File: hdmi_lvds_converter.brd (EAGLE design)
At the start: 100 x 50 mm, 3 parts, among them J602 SS-53000-001, U1 DS90C387VJD/NOPB, U2 TFP401APZP

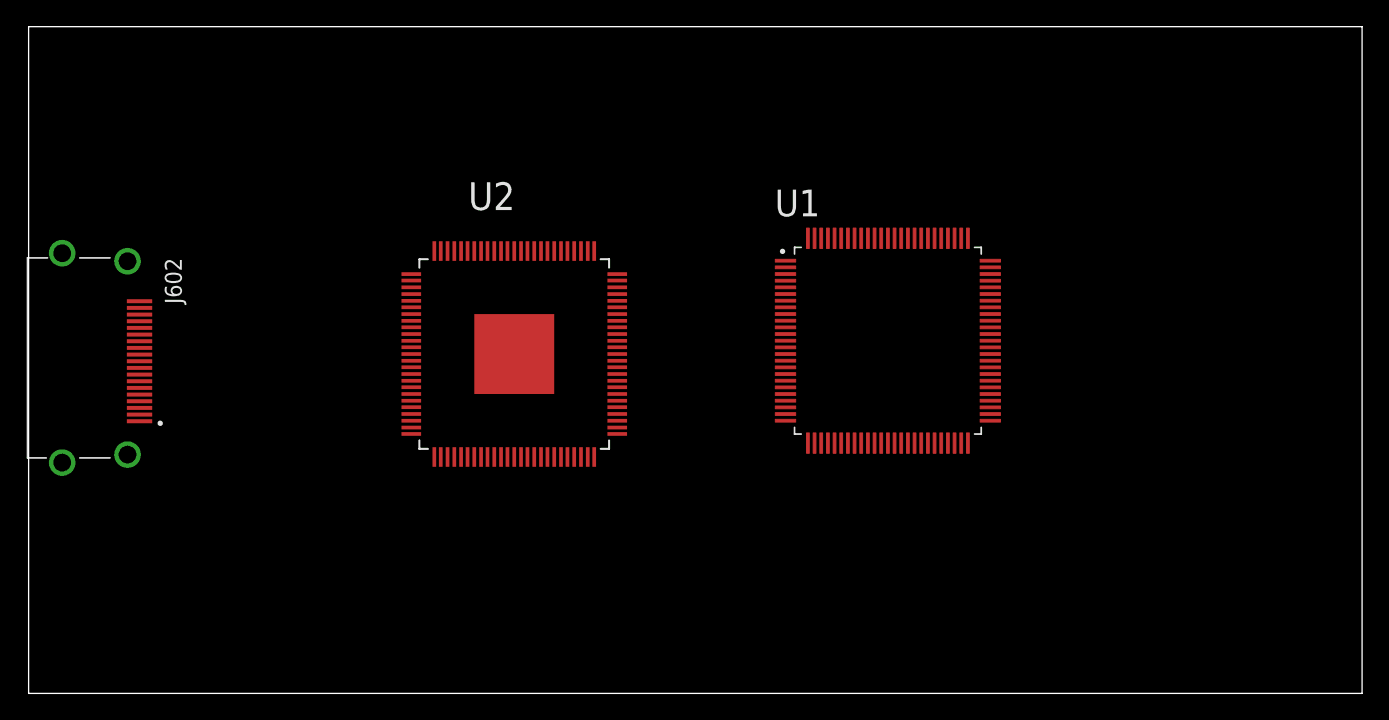
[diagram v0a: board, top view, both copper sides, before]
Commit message: - Change HDMI connector for better layout. - Start routing rgb signals.
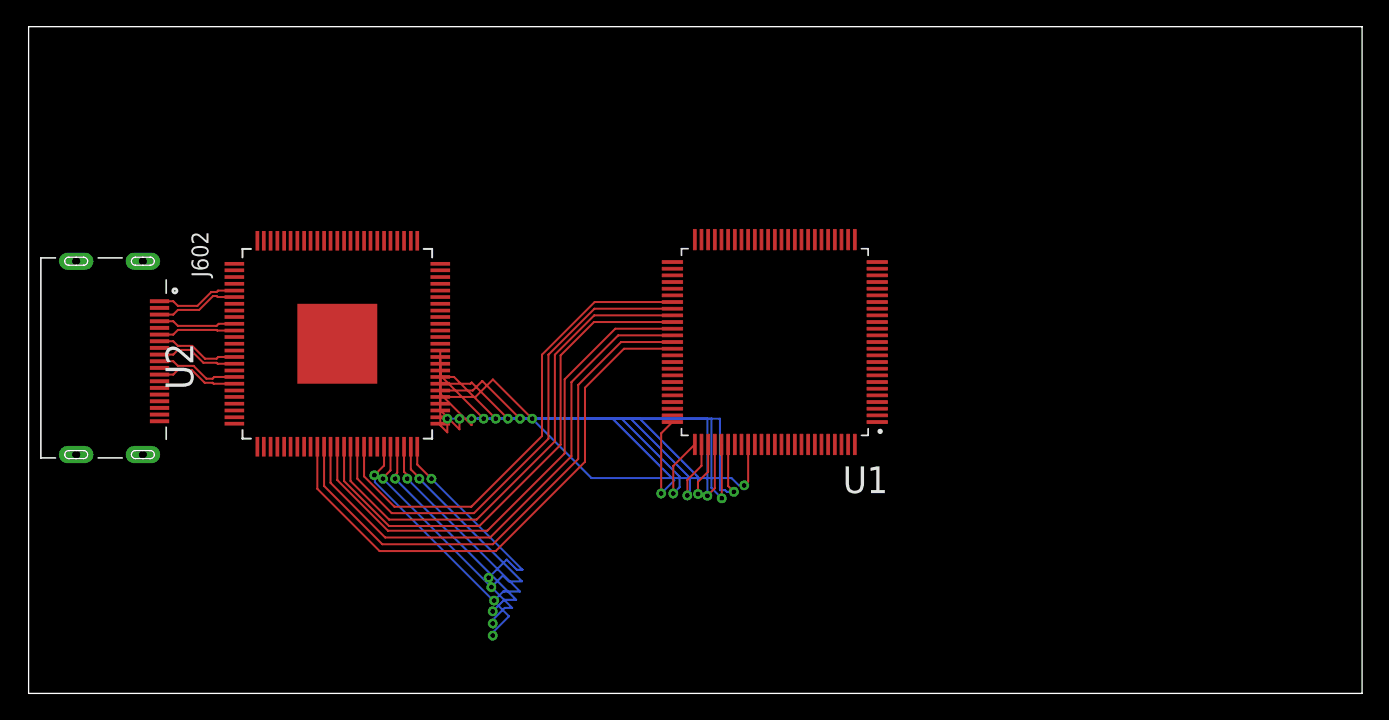
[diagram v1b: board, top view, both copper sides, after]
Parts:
- J602: value SS-53000-001 -> 1759548-2; device ND_main_control_unit:STEWART_SS-53000-001 -> ND_main_control_unit:TE_1759548-2
- moved U2 13.3 mm to (23.1, 26.2), turned to 90 degrees
- moved U1 8.48 mm to (56.0, 26.4), turned to 180 degrees
- moved J602 3.00 mm to (5.32, 25.2)
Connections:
- new net E_B0: U1.64, U2.10
- new net E_B1: U1.63, U2.11
- new net E_B2: U1.62, U2.12
- new net E_B3: U1.61, U2.13
- new net E_B4: U1.60, U2.14
- new net E_B5: U1.59, U2.15
- new net E_B6: U1.58, U2.16
- new net E_B7: U1.57, U2.17
- new net E_G0: U1.74, U2.20
- new net E_G1: U1.73, U2.21
- new net E_G2: U1.72, U2.22
- new net E_G3: U1.71, U2.23
- new net E_G4: U1.70, U2.24
- new net E_G5: U1.69, U2.25
- new net E_G6: U1.66, U2.26
- new net E_G7: U1.65, U2.27
- new net E_R0: U1.84, U2.30
- new net E_R1: U1.81, U2.31
- new net E_R2: U1.80, U2.32
- new net E_R3: U1.79, U2.33
- new net E_R4: U1.78, U2.34
- new net E_R5: U1.77, U2.35
- new net E_R6: U1.76, U2.36
- new net E_R7: U1.75, U2.37
- new net N$25: U2.77
- new net N$26: U2.75
- new net N$27: U2.74
- new net N$28: U2.73
- new net N$29: U2.72
- new net N$30: U2.71
- new net N$31: U2.70
- new net N$32: U2.69
- new net N$33: U2.66
- new net N$34: U2.65
- new net N$35: U2.64
- new net N$36: U2.63
- new net N$37: U2.62
- new net N$38: U2.61
- new net N$39: U2.60
- new net N$40: U2.59
- new net N$41: U2.56
- new net N$42: U2.55
- new net N$43: U2.54
- new net N$44: U2.53
- new net N$45: U2.52
- new net N$46: U2.51
- new net N$47: U2.50
- new net N$48: U2.49
- new net N$57: U1.55
- new net N$58: U1.54
- new net N$59: U1.23
- new net N$60: U1.56
- new net N$61: U1.24
- new net N$62: U1.11
- new net O_B0: U1.92
- new net O_B1: U1.91
- new net O_B2: U1.90
- new net O_B3: U1.89
- new net O_B4: U1.88
- new net O_B5: U1.87
- new net O_B6: U1.86
- new net O_B7: U1.85
- new net O_G0: U1.2
- new net O_G1: U1.1
- new net O_G2: U1.100
- new net O_G3: U1.99
- new net O_G4: U1.96
- new net O_G5: U1.95
- new net O_G6: U1.94
- new net O_G7: U1.93
- new net O_R0: U1.10
- new net O_R1: U1.9
- new net O_R2: U1.8
- new net O_R3: U1.7
- new net O_R4: U1.6
- new net O_R5: U1.5
- new net O_R6: U1.4
- new net O_R7: U1.3
- net GND: now also J602.11, J602.17, J602.2, J602.5, J602.8; no longer J602.1, J602.10, J602.13, J602.4, J602.7
- net HDMI_CEC: now also J602.13; no longer J602.14
- net HDMI_CK_N: now also U2.94
- net HDMI_CK_P: now also J602.10, U2.93; no longer J602.11
- net HDMI_D0_N: now also U2.91
- net HDMI_D0_P: now also J602.7, U2.90; no longer J602.8
- net HDMI_D1_N: now also U2.86
- net HDMI_D1_P: now also J602.4, U2.85; no longer J602.5
- net HDMI_D2_N: now also U2.81
- net HDMI_D2_P: now also J602.1, U2.80; no longer J602.2
- net HDMI_UTIL: now also J602.14; no longer J602.17
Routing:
- net E_B0: track 0.00 -> 41.3 mm
- net E_B1: track 0.00 -> 40.4 mm
- net E_B2: track 0.00 -> 39.6 mm
- net E_B4: track 0.00 -> 38.9 mm
- net E_B3: track 0.00 -> 38.7 mm
- net E_B5: track 0.00 -> 38.1 mm
- net E_B6: track 0.00 -> 37.1 mm
- net E_B7: track 0.00 -> 36.2 mm
- net E_R7: track 0.00 -> 33.4 mm, vias 0 -> 2
- net E_R1: track 0.00 -> 32.6 mm, vias 0 -> 2
- net E_R2: track 0.00 -> 31.8 mm, vias 0 -> 2
- net E_R3: track 0.00 -> 31.2 mm, vias 0 -> 2
- net E_R6: track 0.00 -> 30.9 mm, vias 0 -> 2
- net E_R5: track 0.00 -> 29.9 mm, vias 0 -> 2
- net E_R0: track 0.00 -> 29.8 mm, vias 0 -> 2
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
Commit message: - Start routing LVDS lines.
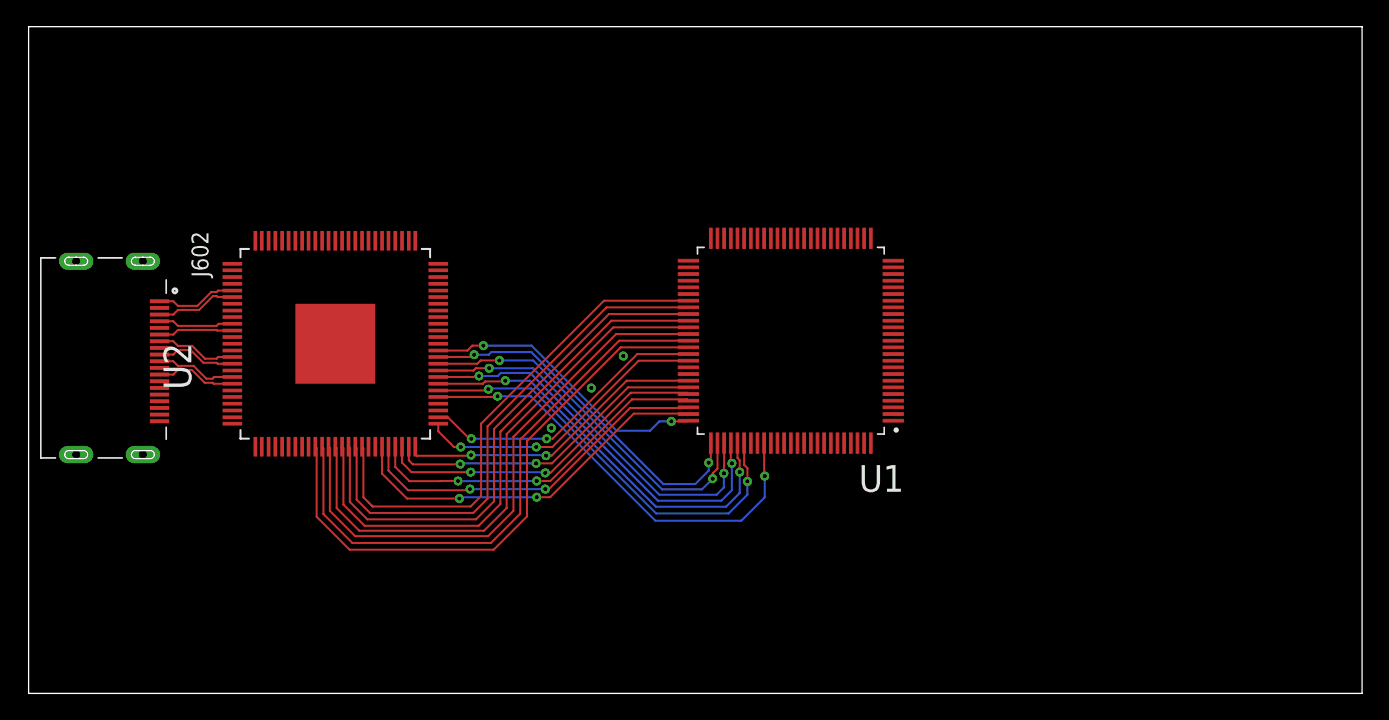
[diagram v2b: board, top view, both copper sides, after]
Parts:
- moved U1 1.20 mm to (57.2, 26.4)
- moved U2 0.15 mm to (23.0, 26.2)
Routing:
- net E_G6: track 0.00 -> 22.5 mm, vias 0 -> 2
- net E_G7: track 0.00 -> 22.1 mm, vias 0 -> 2
- net E_R7: track 33.4 -> 21.9 mm
- net E_G0: track 19.2 -> 28.4 mm
- net E_G2: track 17.4 -> 26.5 mm
- net E_G1: track 18.4 -> 27.5 mm
- net E_G3: track 16.7 -> 25.5 mm
- net E_G4: track 16.4 -> 24.5 mm
- net E_G5: track 15.9 -> 23.5 mm
- net E_R6: track 30.9 -> 27.2 mm
- net E_R0: track 29.8 -> 33.2 mm
- net E_B3: track 38.7 -> 41.3 mm
- net E_B0: track 41.3 -> 43.8 mm
- net E_B2: track 39.6 -> 42.1 mm
- net E_B1: track 40.4 -> 42.9 mm
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
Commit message: - Latest changes
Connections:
- removed net N$25: U2.77
- removed net N$26: U2.75
- removed net N$27: U2.74
- removed net N$28: U2.73
- removed net N$29: U2.72
- removed net N$30: U2.71
- removed net N$31: U2.70
- removed net N$32: U2.69
- removed net N$33: U2.66
- removed net N$34: U2.65
- removed net N$35: U2.64
- removed net N$36: U2.63
- removed net N$37: U2.62
- removed net N$38: U2.61
- removed net N$39: U2.60
- removed net N$40: U2.59
- removed net N$41: U2.56
- removed net N$42: U2.55
- removed net N$43: U2.54
- removed net N$44: U2.53
- removed net N$45: U2.52
- removed net N$46: U2.51
- removed net N$47: U2.50
- removed net N$48: U2.49
- net O_B0: now also U2.49
- net O_B1: now also U2.50
- net O_B2: now also U2.51
- net O_B3: now also U2.52
- net O_B4: now also U2.53
- net O_B5: now also U2.54
- net O_B6: now also U2.55
- net O_B7: now also U2.56
- net O_G0: now also U2.59
- net O_G1: now also U2.60
- net O_G2: now also U2.61
- net O_G3: now also U2.62
- net O_G4: now also U2.63
- net O_G5: now also U2.64
- net O_G6: now also U2.65
- net O_G7: now also U2.66
- net O_R0: now also U2.69
- net O_R1: now also U2.70
- net O_R2: now also U2.71
- net O_R3: now also U2.72
- net O_R4: now also U2.73
- net O_R5: now also U2.74
- net O_R6: now also U2.75
- net O_R7: now also U2.77
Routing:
- net O_R6: track 0.00 -> 81.0 mm
- net O_R0: track 0.00 -> 70.4 mm
- net O_B2: track 0.00 -> 39.1 mm
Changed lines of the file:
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@@
 <wire x1="46.6" y1="19.7" x2="47.3" y2="20.4" width="0.1524" layer="16"/>
-</signal>
-<signal name="N$25">
-<contactref element="U2" pad="77"/>
-</signal>
-<signal name="N$26">
-<contactref element="U2" pad="75"/>
-</signal>
-<signal name="N$27">
-<contactref element="U2" pad="74"/>
-</signal>
-<signal name="N$28">
-<contactref element="U2" pad="73"/>
-</signal>
-<signal name="N$29">
-<contactref element="U2" pad="72"/>
-</signal>
-<signal name="N$30">
-<contactref element="U2" pad="71"/>
-</signal>
-<signal name="N$31">
-<contactref element="U2" pad="70"/>
-</signal>
-<signal name="N$32">
-<contactref element="U2" pad="69"/>
-</signal>
-<signal name="N$33">
-<contactref element="U2" pad="66"/>
-</signal>
-<signal name="N$34">
-<contactref element="U2" pad="65"/>
-</signal>
-<signal name="N$35">
-<contactref element="U2" pad="64"/>
-</signal>
-<signal name="N$36">
-<contactref element="U2" pad="63"/>
-</signal>
-<signal name="N$37">
-<contactref element="U2" pad="62"/>
-</signal>
-<signal name="N$38">
-<contactref element="U2" pad="61"/>
-</signal>
-<signal name="N$39">
-<contactref element="U2" pad="60"/>
-</signal>
-<signal name="N$40">
-<contactref element="U2" pad="59"/>
-</signal>
-<signal name="N$41">
-<contactref element="U2" pad="56"/>
-</signal>
-<signal name="N$42">
-<contactref element="U2" pad="55"/>
-</signal>
-<signal name="N$43">
-<contactref element="U2" pad="54"/>
-</signal>
-<signal name="N$44">
-<contactref element="U2" pad="53"/>
-</signal>
-<signal name="N$45">
-<contactref element="U2" pad="52"/>
-</signal>
-<signal name="N$46">
-<contactref element="U2" pad="51"/>
-</signal>
-<signal name="N$47">
-<contactref element="U2" pad="50"/>
-</signal>
-<signal name="N$48">
-<contactref element="U2" pad="49"/>
 </signal>
 <signal name="E_G3">
@@
 <signal name="O_R7">
 <contactref element="U1" pad="3"/>
+<contactref element="U2" pad="77"/>
+<wire x1="15.2784" y1="31.7318" x2="64.84" y2="21.45" width="0" layer="19" extent="1-1"/>
 </signal>
 <signal name="O_R6">
 <contactref element="U1" pad="4"/>
+<contactref element="U2" pad="75"/>
+<wire x1="17.0056" y1="33.9416" x2="17.0056" y2="35.9056" width="0.1524" layer="1"/>
+<wire x1="17.0056" y1="35.9056" x2="23.9" y2="42.8" width="0.1524" layer="1"/>
+<wire x1="23.9" y1="42.8" x2="65.9" y2="42.8" width="0.1524" layer="1"/>
+<wire x1="65.9" y1="42.8" x2="71.6" y2="37.1" width="0.1524" layer="1"/>
+<wire x1="71.6" y1="37.1" x2="71.6" y2="26.6" width="0.1524" layer="1"/>
+<wire x1="66.95" y1="21.95" x2="64.84" y2="21.95" width="0.1524" layer="1"/>
+<wire x1="71.6" y1="26.6" x2="66.95" y2="21.95" width="0.1524" layer="1"/>
 </signal>
 <signal name="O_R5">
 <contactref element="U1" pad="5"/>
+<contactref element="U2" pad="74"/>
+<wire x1="17.4882" y1="33.9416" x2="64.84" y2="22.45" width="0" layer="19" extent="1-1"/>
 </signal>
 <signal name="O_R4">
 <contactref element="U1" pad="6"/>
+<contactref element="U2" pad="73"/>
+<wire x1="17.9962" y1="33.9416" x2="64.84" y2="22.95" width="0" layer="19" extent="1-1"/>
 </signal>
 <signal name="O_R3">
 <contactref element="U1" pad="7"/>
+<contactref element="U2" pad="72"/>
+<wire x1="18.5042" y1="33.9416" x2="64.84" y2="23.45" width="0" layer="19" extent="1-1"/>
 </signal>
 <signal name="O_R2">
 <contactref element="U1" pad="8"/>
+<contactref element="U2" pad="71"/>
+<wire x1="19.0122" y1="33.9416" x2="64.84" y2="23.95" width="0" layer="19" extent="1-1"/>
 </signal>
 <signal name="O_R1">
 <contactref element="U1" pad="9"/>
+<contactref element="U2" pad="70"/>
+<wire x1="19.4948" y1="33.9416" x2="64.84" y2="24.45" width="0" layer="19" extent="1-1"/>
 </signal>
 <signal name="O_R0">
 <contactref element="U1" pad="10"/>
+<contactref element="U2" pad="69"/>
+<wire x1="20.0028" y1="33.9416" x2="20.0028" y2="36.1028" width="0.1524" layer="1"/>
+<wire x1="69.8" y1="36.5" x2="69.8" y2="27.9" width="0.1524" layer="1"/>
+<wire x1="69.8" y1="27.9" x2="66.85" y2="24.95" width="0.1524" layer="1"/>
+<wire x1="66.85" y1="24.95" x2="64.84" y2="24.95" width="0.1524" layer="1"/>
+<wire x1="20.0028" y1="36.1028" x2="24.6" y2="40.7" width="0.1524" layer="1"/>
+<wire x1="24.6" y1="40.7" x2="65.6" y2="40.7" width="0.1524" layer="1"/>
+<wire x1="65.6" y1="40.7" x2="69.8" y2="36.5" width="0.1524" layer="1"/>
 </signal>
 <signal name="O_G7">
 <contactref element="U1" pad="93"/>
+<contactref element="U2" pad="66"/>
+<wire x1="21.5014" y1="33.9416" x2="59.66" y2="18.77" width="0" layer="19" extent="1-1"/>
 </signal>
 <signal name="O_G6">
 <contactref element="U1" pad="94"/>
+<contactref element="U2" pad="65"/>
+<wire x1="22.0094" y1="33.9416" x2="60.16" y2="18.77" width="0" layer="19" extent="1-1"/>
 </signal>
 <signal name="O_G5">
 <contactref element="U1" pad="95"/>
+<contactref element="U2" pad="64"/>
+<wire x1="22.492" y1="33.9416" x2="60.66" y2="18.77" width="0" layer="19" extent="1-1"/>
 </signal>
 <signal name="O_G4">
 <contactref element="U1" pad="96"/>
+<contactref element="U2" pad="63"/>
+<wire x1="23" y1="33.9416" x2="61.16" y2="18.77" width="0" layer="19" extent="1-1"/>
 </signal>
 <signal name="O_G3">
 <contactref element="U1" pad="99"/>
+<contactref element="U2" pad="62"/>
+<wire x1="23.508" y1="33.9416" x2="62.66" y2="18.77" width="0" layer="19" extent="1-1"/>
 </signal>
 <signal name="O_G2">
 <contactref element="U1" pad="100"/>
+<contactref element="U2" pad="61"/>
+<wire x1="23.9906" y1="33.9416" x2="63.16" y2="18.77" width="0" layer="19" extent="1-1"/>
 </signal>
 <signal name="O_G1">
 <contactref element="U1" pad="1"/>
+<contactref element="U2" pad="60"/>
+<wire x1="24.4986" y1="33.9416" x2="64.84" y2="20.45" width="0" layer="19" extent="1-1"/>
 </signal>
 <signal name="O_G0">
 <contactref element="U1" pad="2"/>
+<contactref element="U2" pad="59"/>
+<wire x1="25.0066" y1="33.9416" x2="64.84" y2="20.95" width="0" layer="19" extent="1-1"/>
 </signal>
 <signal name="N$57">
@@
 <signal name="O_B7">
 <contactref element="U1" pad="85"/>
+<contactref element="U2" pad="56"/>
+<wire x1="26.5052" y1="33.9416" x2="55.66" y2="18.77" width="0" layer="19" extent="1-1"/>
 </signal>
 <signal name="O_B6">
 <contactref element="U1" pad="86"/>
+<contactref element="U2" pad="55"/>
+<wire x1="26.9878" y1="33.9416" x2="56.16" y2="18.77" width="0" layer="19" extent="1-1"/>
 </signal>
 <signal name="O_B5">
 <contactref element="U1" pad="87"/>
+<contactref element="U2" pad="54"/>
+<wire x1="27.4958" y1="33.9416" x2="56.66" y2="18.77" width="0" layer="19" extent="1-1"/>
 </signal>
 <signal name="O_B4">
 <contactref element="U1" pad="88"/>
+<contactref element="U2" pad="53"/>
+<wire x1="28.0038" y1="33.9416" x2="57.16" y2="18.77" width="0" layer="19" extent="1-1"/>
 </signal>
 <signal name="O_B3">
 <contactref element="U1" pad="89"/>
+<contactref element="U2" pad="52"/>
+<wire x1="28.5118" y1="33.9416" x2="57.66" y2="18.77" width="0" layer="19" extent="1-1"/>
 </signal>
 <signal name="O_B2">
 <contactref element="U1" pad="90"/>
+<contactref element="U2" pad="51"/>
+<wire x1="50.5086" y1="32.6641875" x2="50.5086" y2="30.6914" width="0.1524" layer="1"/>
+<wire x1="28.9944" y1="33.9416" x2="49.2311875" y2="33.9416" width="0.1524" layer="1"/>
+<wire x1="49.2311875" y1="33.9416" x2="50.5086" y2="32.6641875" width="0.1524" layer="1"/>
+<wire x1="58.16" y1="23.04" x2="58.16" y2="18.77" width="0.1524" layer="1"/>
+<wire x1="50.5086" y1="30.6914" x2="58.16" y2="23.04" width="0.1524" layer="1"/>
 </signal>
 <signal name="O_B1">
 <contactref element="U1" pad="91"/>
+<contactref element="U2" pad="50"/>
+<wire x1="30.7216" y1="32.2144" x2="58.66" y2="18.77" width="0" layer="19" extent="1-1"/>
 </signal>
 <signal name="O_B0">
 <contactref element="U1" pad="92"/>
+<contactref element="U2" pad="49"/>
+<wire x1="30.7216" y1="31.7318" x2="59.16" y2="18.77" width="0" layer="19" extent="1-1"/>
 </signal>
 <signal name="N$1">
